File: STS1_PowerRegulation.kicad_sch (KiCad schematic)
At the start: 24 parts, among them U24 MCP1725-3302E_MC, U3 MCP1725-3302E_MC

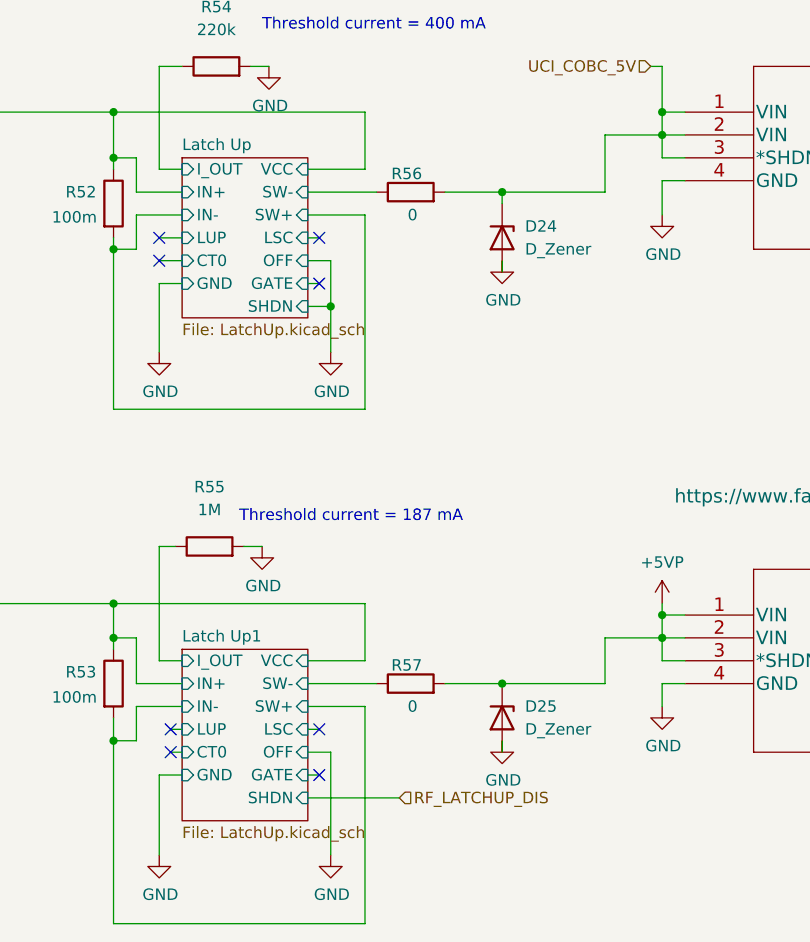
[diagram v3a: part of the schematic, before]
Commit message: Add slew-rate control capacitors to latch-up protection circuits
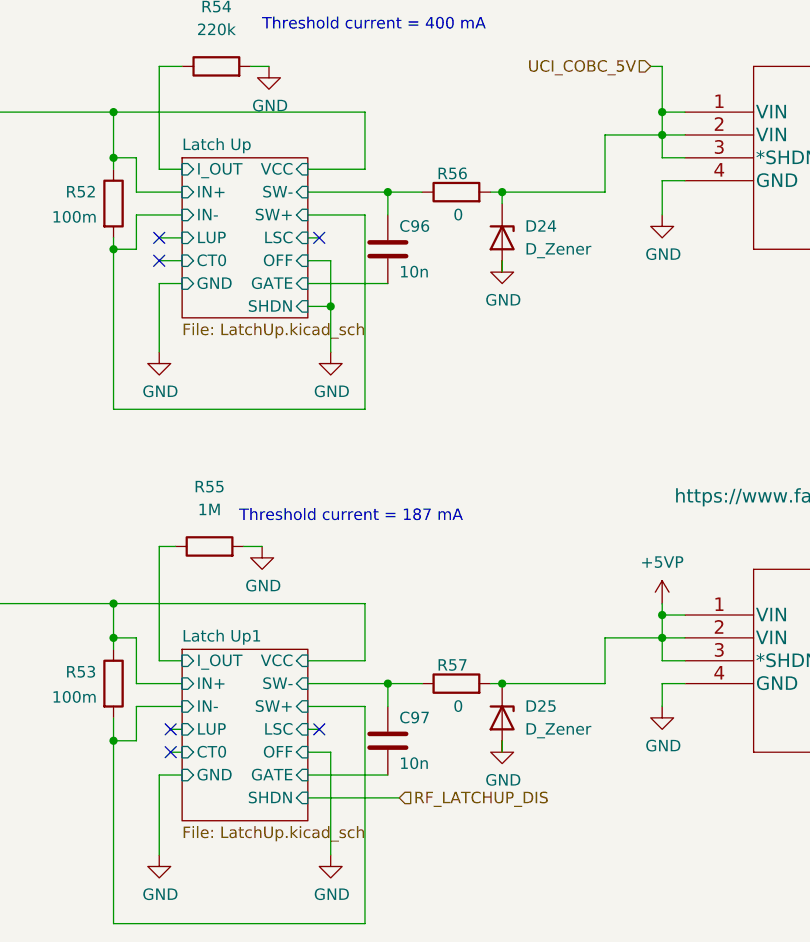
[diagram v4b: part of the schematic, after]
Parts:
- added C96, C97: 10n, Capacitor_SMD:C_0603_1608Metric, symbol Device:C
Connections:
- net Latch Up/GATE: now also C96.2
- net Latch Up/SW-: now also C96.1
- net Latch Up1/GATE: now also C97.2
- net Latch Up1/SW-: now also C97.1
- no-connect marks 12 -> 10
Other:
- moved on the sheet: R56, R57
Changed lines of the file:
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@@
 (kicad_sch (version 20211123) (generator eeschema)
   (paper "A4")
+  (junction (at 95.25 53.34) (diameter 0) (color 0 0 0 0)
+  )
+  (junction (at 125.73 101.6) (diameter 0) (color 0 0 0 0)
+  )
+  (junction (at 212.09 96.52) (diameter 0) (color 0 0 0 0)
+  )
+  (junction (at 95.25 43.18) (diameter 0) (color 0 0 0 0)
+  )
+  (junction (at 74.93 80.01) (diameter 0) (color 0 0 0 0)
+  )
+  (junction (at 227.33 40.64) (diameter 0) (color 0 0 0 0)
+  )
+  (junction (at 156.21 96.52) (diameter 0) (color 0 0 0 0)
+  )
+  (junction (at 95.25 38.1) (diameter 0) (color 0 0 0 0)
+  )
+  (junction (at 125.73 46.99) (diameter 0) (color 0 0 0 0)
+  )
+  (junction (at 156.21 38.1) (diameter 0) (color 0 0 0 0)
+  )
+  (junction (at 156.21 40.64) (diameter 0) (color 0 0 0 0)
+  )
   (junction (at 138.43 101.6) (diameter 0) (color 0 0 0 0)
-  )
-  (junction (at 95.25 53.34) (diameter 0) (color 0 0 0 0)
-  )
-  (junction (at 212.09 96.52) (diameter 0) (color 0 0 0 0)
-  )
-  (junction (at 95.25 43.18) (diameter 0) (color 0 0 0 0)
-  )
-  (junction (at 74.93 80.01) (diameter 0) (color 0 0 0 0)
-  )
-  (junction (at 227.33 40.64) (diameter 0) (color 0 0 0 0)
-  )
-  (junction (at 156.21 96.52) (diameter 0) (color 0 0 0 0)
-  )
-  (junction (at 95.25 38.1) (diameter 0) (color 0 0 0 0)
-  )
-  (junction (at 156.21 38.1) (diameter 0) (color 0 0 0 0)
-  )
-  (junction (at 156.21 40.64) (diameter 0) (color 0 0 0 0)
   )
   (junction (at 69.85 80.01) (diameter 0) (color 0 0 0 0)
@@
   (no_connect (at 118.11 52.07))
   (no_connect (at 118.11 106.68))
-  (no_connect (at 118.11 57.15))
   (no_connect (at 209.55 45.72))
   (no_connect (at 101.6 106.68))
@@
   (no_connect (at 209.55 101.6))
   (no_connect (at 101.6 109.22))
-  (no_connect (at 118.11 111.76))
-  (wire (pts (xy 132.08 101.6) (xy 138.43 101.6))
-    (stroke (width 0) (type default) (color 0 0 0 0))
-  )
-  (wire (pts (xy 132.08 46.99) (xy 138.43 46.99))
+  (wire (pts (xy 137.16 46.99) (xy 138.43 46.99))
     (stroke (width 0) (type default) (color 0 0 0 0))
   )
@@
     (stroke (width 0) (type default) (color 0 0 0 0))
   )
-  (wire (pts (xy 116.84 111.76) (xy 118.11 111.76))
+  (wire (pts (xy 116.84 111.76) (xy 125.73 111.76))
     (stroke (width 0) (type default) (color 0 0 0 0))
   )
@@
     (stroke (width 0) (type default) (color 0 0 0 0))
   )
+  (wire (pts (xy 137.16 101.6) (xy 138.43 101.6))
+    (stroke (width 0) (type default) (color 0 0 0 0))
+  )
   (wire (pts (xy 156.21 40.64) (xy 158.75 40.64))
     (stroke (width 0) (type default) (color 0 0 0 0))
@@
     (stroke (width 0) (type default) (color 0 0 0 0))
   )
-  (wire (pts (xy 116.84 46.99) (xy 124.46 46.99))
+  (wire (pts (xy 125.73 46.99) (xy 129.54 46.99))
+    (stroke (width 0) (type default) (color 0 0 0 0))
+  )
+  (wire (pts (xy 116.84 46.99) (xy 125.73 46.99))
+    (stroke (width 0) (type default) (color 0 0 0 0))
+  )
+  (wire (pts (xy 125.73 46.99) (xy 125.73 49.53))
     (stroke (width 0) (type default) (color 0 0 0 0))
   )
@@
     (stroke (width 0) (type default) (color 0 0 0 0))
   )
-  (wire (pts (xy 116.84 101.6) (xy 124.46 101.6))
+  (wire (pts (xy 116.84 101.6) (xy 125.73 101.6))
     (stroke (width 0) (type default) (color 0 0 0 0))
   )
@@
     (stroke (width 0) (type default) (color 0 0 0 0))
   )
+  (wire (pts (xy 125.73 101.6) (xy 125.73 104.14))
+    (stroke (width 0) (type default) (color 0 0 0 0))
+  )
   (wire (pts (xy 158.75 43.18) (xy 156.21 43.18))
     (stroke (width 0) (type default) (color 0 0 0 0))
@@
     (stroke (width 0) (type default) (color 0 0 0 0))
   )
+  (wire (pts (xy 125.73 101.6) (xy 129.54 101.6))
+    (stroke (width 0) (type default) (color 0 0 0 0))
+  )
   (wire (pts (xy 116.84 106.68) (xy 118.11 106.68))
     (stroke (width 0) (type default) (color 0 0 0 0))
   )
-  (wire (pts (xy 116.84 57.15) (xy 118.11 57.15))
+  (wire (pts (xy 116.84 57.15) (xy 125.73 57.15))
     (stroke (width 0) (type default) (color 0 0 0 0))
   )
@@
     (pin "2")
   )
-  (symbol (lib_id "Device:R") (at 128.27 46.99 90) (unit 1)
-    (in_bom yes) (on_board yes)
-    (property "Reference" "R56" (id 0) (at 129.54 44.958 90)
-      (effects (font (size 1.27 1.27)) (justify left))
-    )
-    (property "Value" "0" (id 1) (at 129.032 49.53 90)
-      (effects (font (size 1.27 1.27)) (justify left))
-    )
-    (property "Footprint" "Resistor_SMD:R_0603_1608Metric" (id 2) (at 128.27 48.768 90)
-      (effects (font (size 1.27 1.27)) hide)
-    )
-    (property "Datasheet" "~" (id 3) (at 128.27 46.99 0)
-      (effects (font (size 1.27 1.27)) hide)
-    )
-    (property "JLCPCB Part #" "C4117710" (id 4) (at 128.27 46.99 0)
-      (effects (font (size 1.27 1.27)) hide)
-    )
-    (property "Manufacturer_Part_Number" "ERJ-H3G0R00V" (id 5) (at 128.27 46.99 0)
+  (symbol (lib_id "Device:R") (at 133.35 46.99 90) (unit 1)
+    (in_bom yes) (on_board yes)
+    (property "Reference" "R56" (id 0) (at 134.62 44.958 90)
+      (effects (font (size 1.27 1.27)) (justify left))
+    )
+    (property "Value" "0" (id 1) (at 134.112 49.53 90)
+      (effects (font (size 1.27 1.27)) (justify left))
+    )
+    (property "Footprint" "Resistor_SMD:R_0603_1608Metric" (id 2) (at 133.35 48.768 90)
+      (effects (font (size 1.27 1.27)) hide)
+    )
+    (property "Datasheet" "~" (id 3) (at 133.35 46.99 0)
+      (effects (font (size 1.27 1.27)) hide)
+    )
+    (property "JLCPCB Part #" "C4117710" (id 4) (at 133.35 46.99 0)
+      (effects (font (size 1.27 1.27)) hide)
+    )
+    (property "Manufacturer_Part_Number" "ERJ-H3G0R00V" (id 5) (at 133.35 46.99 0)
       (effects (font (size 1.27 1.27)) hide)
     )
@@
     (pin "1")
   )
-  (symbol (lib_id "Device:R") (at 128.27 101.6 90) (unit 1)
-    (in_bom yes) (on_board yes)
-    (property "Reference" "R57" (id 0) (at 129.54 99.568 90)
-      (effects (font (size 1.27 1.27)) (justify left))
-    )
-    (property "Value" "0" (id 1) (at 129.032 104.14 90)
-      (effects (font (size 1.27 1.27)) (justify left))
-    )
-    (property "Footprint" "Resistor_SMD:R_0603_1608Metric" (id 2) (at 128.27 103.378 90)
-      (effects (font (size 1.27 1.27)) hide)
-    )
-    (property "Datasheet" "~" (id 3) (at 128.27 101.6 0)
-      (effects (font (size 1.27 1.27)) hide)
-    )
-    (property "JLCPCB Part #" "C4117710" (id 4) (at 128.27 101.6 0)
-      (effects (font (size 1.27 1.27)) hide)
-    )
-    (property "Manufacturer_Part_Number" "ERJ-H3G0R00V" (id 5) (at 128.27 101.6 0)
+  (symbol (lib_id "Device:R") (at 133.35 101.6 90) (unit 1)
+    (in_bom yes) (on_board yes)
+    (property "Reference" "R57" (id 0) (at 134.62 99.568 90)
+      (effects (font (size 1.27 1.27)) (justify left))
+    )
+    (property "Value" "0" (id 1) (at 134.112 104.14 90)
+      (effects (font (size 1.27 1.27)) (justify left))
+    )
+    (property "Footprint" "Resistor_SMD:R_0603_1608Metric" (id 2) (at 133.35 103.378 90)
+      (effects (font (size 1.27 1.27)) hide)
+    )
+    (property "Datasheet" "~" (id 3) (at 133.35 101.6 0)
+      (effects (font (size 1.27 1.27)) hide)
+    )
+    (property "JLCPCB Part #" "C4117710" (id 4) (at 133.35 101.6 0)
+      (effects (font (size 1.27 1.27)) hide)
+    )
+    (property "Manufacturer_Part_Number" "ERJ-H3G0R00V" (id 5) (at 133.35 101.6 0)
       (effects (font (size 1.27 1.27)) hide)
     )
@@
     (pin "1")
   )
+  (symbol (lib_id "Device:C") (at 125.73 53.34 0) (unit 1)
+    (in_bom yes) (on_board yes)
+    (property "Reference" "C96" (id 0) (at 127 50.8 0)
+      (effects (font (size 1.27 1.27)) (justify left))
+    )
+    (property "Value" "10n" (id 1) (at 127 55.88 0)
+      (effects (font (size 1.27 1.27)) (justify left))
+    )
+    (property "Footprint" "Capacitor_SMD:C_0603_1608Metric" (id 2) (at 126.6952 57.15 0)
+      (effects (font (size 1.27 1.27)) hide)
+    )
+    (property "Datasheet" "~" (id 3) (at 125.73 53.34 0)
+      (effects (font (size 1.27 1.27)) hide)
+    )
+    (property "JLCPCB Part #" "C307477" (id 4) (at 125.73 53.34 0)
+      (effects (font (size 1.27 1.27)) hide)
+    )
+    (property "Manufacturer_Part_Number" "CL10B103KB8NFNC " (id 5) (at 125.73 53.34 0)
+      (effects (font (size 1.27 1.27)) hide)
+    )
+    (pin "1")
+    (pin "2")
+  )
   (symbol (lib_id "Connector:TestPoint") (at 242.57 93.98 0) (unit 1)
     (in_bom no) (on_board yes)
@@
     (pin "1")
   )
+  (symbol (lib_id "Device:C") (at 125.73 107.95 0) (unit 1)
+    (in_bom yes) (on_board yes)
+    (property "Reference" "C97" (id 0) (at 127 105.41 0)
+      (effects (font (size 1.27 1.27)) (justify left))
+    )
+    (property "Value" "10n" (id 1) (at 127 110.49 0)
+      (effects (font (size 1.27 1.27)) (justify left))
+    )
+    (property "Footprint" "Capacitor_SMD:C_0603_1608Metric" (id 2) (at 126.6952 111.76 0)
+      (effects (font (size 1.27 1.27)) hide)
+    )
+    (property "Datasheet" "~" (id 3) (at 125.73 107.95 0)
+      (effects (font (size 1.27 1.27)) hide)
+    )
+    (property "JLCPCB Part #" "C307477" (id 4) (at 125.73 107.95 0)
+      (effects (font (size 1.27 1.27)) hide)
+    )
+    (property "Manufacturer_Part_Number" "CL10B103KB8NFNC " (id 5) (at 125.73 107.95 0)
+      (effects (font (size 1.27 1.27)) hide)
+    )
+    (pin "1")
+    (pin "2")
+  )
   (sheet (at 102.87 43.18) (size 13.97 17.78) (fields_autoplaced)

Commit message: Add a defined state (pulled to GND) of the output of LT1336 for the case when it is a shutdown state
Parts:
- added R75: 10k, Resistor_SMD:R_0603_1608Metric, symbol Device:R
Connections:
- net GND: now also R75.2
- net Latch Up1/LUP: now also R75.1
- no-connect marks 10 -> 9
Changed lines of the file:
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@@
   (no_connect (at 118.11 106.68))
   (no_connect (at 209.55 45.72))
-  (no_connect (at 101.6 106.68))
   (no_connect (at 100.33 52.07))
   (no_connect (at 209.55 48.26))
@@
     (stroke (width 0) (type default) (color 0 0 0 0))
   )
+  (wire (pts (xy 86.36 109.22) (xy 86.36 106.68))
+    (stroke (width 0) (type default) (color 0 0 0 0))
+  )
   (wire (pts (xy 110.49 33.02) (xy 112.522 33.02))
     (stroke (width 0) (type default) (color 0 0 0 0))
@@
     (stroke (width 0) (type default) (color 0 0 0 0))
   )
-  (wire (pts (xy 101.6 106.68) (xy 102.87 106.68))
+  (wire (pts (xy 86.36 106.68) (xy 102.87 106.68))
     (stroke (width 0) (type default) (color 0 0 0 0))
   )
@@
   )
   (wire (pts (xy 212.09 96.52) (xy 227.33 96.52))
+    (stroke (width 0) (type default) (color 0 0 0 0))
+  )
+  (wire (pts (xy 86.36 116.84) (xy 86.36 120.65))
     (stroke (width 0) (type default) (color 0 0 0 0))
   )
@@
     (pin "1")
   )
+  (symbol (lib_id "power:GND") (at 86.36 120.65 0) (unit 1)
+    (in_bom yes) (on_board yes)
+    (property "Reference" "#PWR064" (id 0) (at 86.36 127 0)
+      (effects (font (size 1.27 1.27)) hide)
+    )
+    (property "Value" "GND" (id 1) (at 86.487 125.0442 0))
+    (property "Footprint" "" (id 2) (at 86.36 120.65 0)
+      (effects (font (size 1.27 1.27)) hide)
+    )
+    (property "Datasheet" "" (id 3) (at 86.36 120.65 0)
+      (effects (font (size 1.27 1.27)) hide)
+    )
+    (pin "1")
+  )
   (symbol (lib_id "power:+3V3") (at 46.228 24.892 0) (unit 1)
     (in_bom yes) (on_board yes) (fields_autoplaced)
@@
     (pin "1")
   )
+  (symbol (lib_id "Device:R") (at 86.36 113.03 0) (unit 1)
+    (in_bom yes) (on_board yes)
+    (property "Reference" "R75" (id 0) (at 83.82 111.76 0)
+      (effects (font (size 1.27 1.27)) (justify right))
+    )
+    (property "Value" "10k" (id 1) (at 83.82 114.3 0)
+      (effects (font (size 1.27 1.27)) (justify right))
+    )
+    (property "Footprint" "Resistor_SMD:R_0603_1608Metric" (id 2) (at 84.582 113.03 90)
+      (effects (font (size 1.27 1.27)) hide)
+    )
+    (property "Datasheet" "~" (id 3) (at 86.36 113.03 0)
+      (effects (font (size 1.27 1.27)) hide)
+    )
+    (property "JLCPCB Part #" "C4297913" (id 4) (at 86.36 113.03 0)
+      (effects (font (size 1.27 1.27)) hide)
+    )
+    (property "Manufacturer_Part_Number" "ERJ-H3EF1002V" (id 5) (at 86.36 113.03 0)
+      (effects (font (size 1.27 1.27)) hide)
+    )
+    (pin "1")
+    (pin "2")
+  )
   (symbol (lib_id "Device:R") (at 106.68 33.02 90) (unit 1)

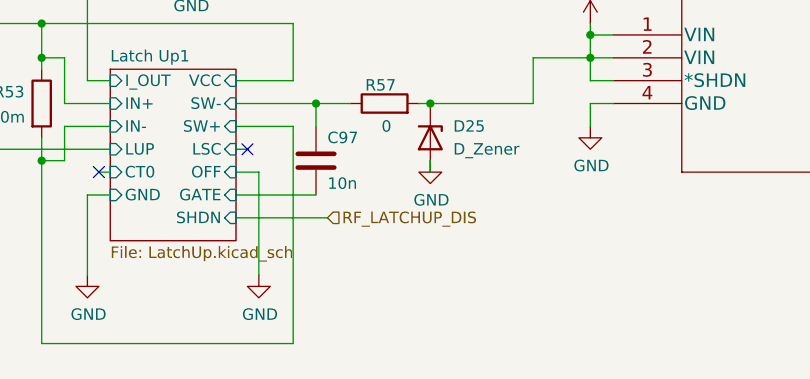
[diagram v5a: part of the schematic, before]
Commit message: Add a pull down resistor to RF_LATCHUP_DIS input
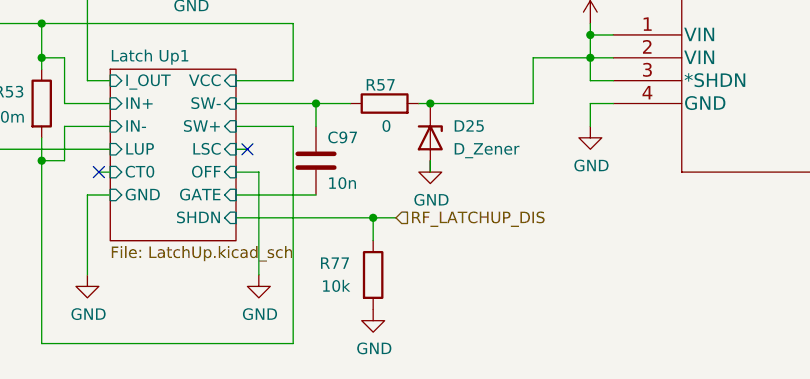
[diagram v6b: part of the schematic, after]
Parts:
- added R77: 10k, Resistor_SMD:R_0603_1608Metric, symbol Device:R
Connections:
- net GND: now also R77.2
- net RF_LATCHUP_DIS: now also R77.1
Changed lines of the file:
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@@
   (junction (at 95.25 107.95) (diameter 0) (color 0 0 0 0)
+  )
+  (junction (at 132.08 114.3) (diameter 0) (color 0 0 0 0)
   )
   (junction (at 234.95 96.52) (diameter 0) (color 0 0 0 0)
@@
     (stroke (width 0) (type default) (color 0 0 0 0))
   )
+  (wire (pts (xy 132.08 114.3) (xy 132.08 116.84))
+    (stroke (width 0) (type default) (color 0 0 0 0))
+  )
   (wire (pts (xy 109.728 86.36) (xy 111.76 86.36))
     (stroke (width 0) (type default) (color 0 0 0 0))
@@
     (stroke (width 0) (type default) (color 0 0 0 0))
   )
-  (wire (pts (xy 116.84 114.3) (xy 127 114.3))
+  (wire (pts (xy 116.84 114.3) (xy 132.08 114.3))
     (stroke (width 0) (type default) (color 0 0 0 0))
   )
@@
   )
   (wire (pts (xy 209.55 40.64) (xy 212.09 40.64))
+    (stroke (width 0) (type default) (color 0 0 0 0))
+  )
+  (wire (pts (xy 132.08 114.3) (xy 134.62 114.3))
     (stroke (width 0) (type default) (color 0 0 0 0))
   )
@@
     (effects (font (size 1.27 1.27)) (justify left bottom))
   )
-  (hierarchical_label "RF_LATCHUP_DIS" (shape input) (at 127 114.3 0)
+  (hierarchical_label "RF_LATCHUP_DIS" (shape input) (at 134.62 114.3 0)
     (effects (font (size 1.27 1.27)) (justify left))
   )
@@
     (pin "9")
   )
+  (symbol (lib_id "Device:R") (at 132.08 120.65 0) (unit 1)
+    (in_bom yes) (on_board yes)
+    (property "Reference" "R77" (id 0) (at 129.54 119.38 0)
+      (effects (font (size 1.27 1.27)) (justify right))
+    )
+    (property "Value" "10k" (id 1) (at 129.54 121.92 0)
+      (effects (font (size 1.27 1.27)) (justify right))
+    )
+    (property "Footprint" "Resistor_SMD:R_0603_1608Metric" (id 2) (at 130.302 120.65 90)
+      (effects (font (size 1.27 1.27)) hide)
+    )
+    (property "Datasheet" "~" (id 3) (at 132.08 120.65 0)
+      (effects (font (size 1.27 1.27)) hide)
+    )
+    (property "JLCPCB Part #" "C4297913" (id 4) (at 132.08 120.65 0)
+      (effects (font (size 1.27 1.27)) hide)
+    )
+    (property "Manufacturer_Part_Number" "ERJ-H3EF1002V" (id 5) (at 132.08 120.65 0)
+      (effects (font (size 1.27 1.27)) hide)
+    )
+    (pin "1")
+    (pin "2")
+  )
   (symbol (lib_id "power:GND") (at 119.38 64.77 0) (unit 1)
     (in_bom yes) (on_board yes)
@@
       (effects (font (size 1.27 1.27)) hide)
     )
+    (pin "1")
+  )
+  (symbol (lib_id "power:GND") (at 132.08 124.46 0) (unit 1)
+    (in_bom yes) (on_board yes)
+    (property "Reference" "#PWR082" (id 0) (at 132.08 130.81 0)
+      (effects (font (size 1.27 1.27)) hide)
+    )
+    (property "Value" "GND" (id 1) (at 132.207 128.8542 0))
+    (property "Footprint" "" (id 2) (at 132.08 124.46 0)
+      (effects (font (size 1.27 1.27)) hide)
+    )
+    (property "Datasheet" "" (id 3) (at 132.08 124.46 0)
+      (effects (font (size 1.27 1.27)) hide)
+    )
